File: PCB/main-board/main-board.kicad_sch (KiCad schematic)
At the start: 91 parts, among them J1 AudioJack2_Ground_Switch, J2 AudioJack2_Ground_Switch, J3 AudioJack2_Ground_Switch, J4 AudioJack2_Ground_Switch, J5 AudioJack2_Ground_Switch, J6 Conn_01x14, J7 Conn_01x03, Q1 Si1308EDL, Q10 Si1308EDL, Q11 DMG2305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

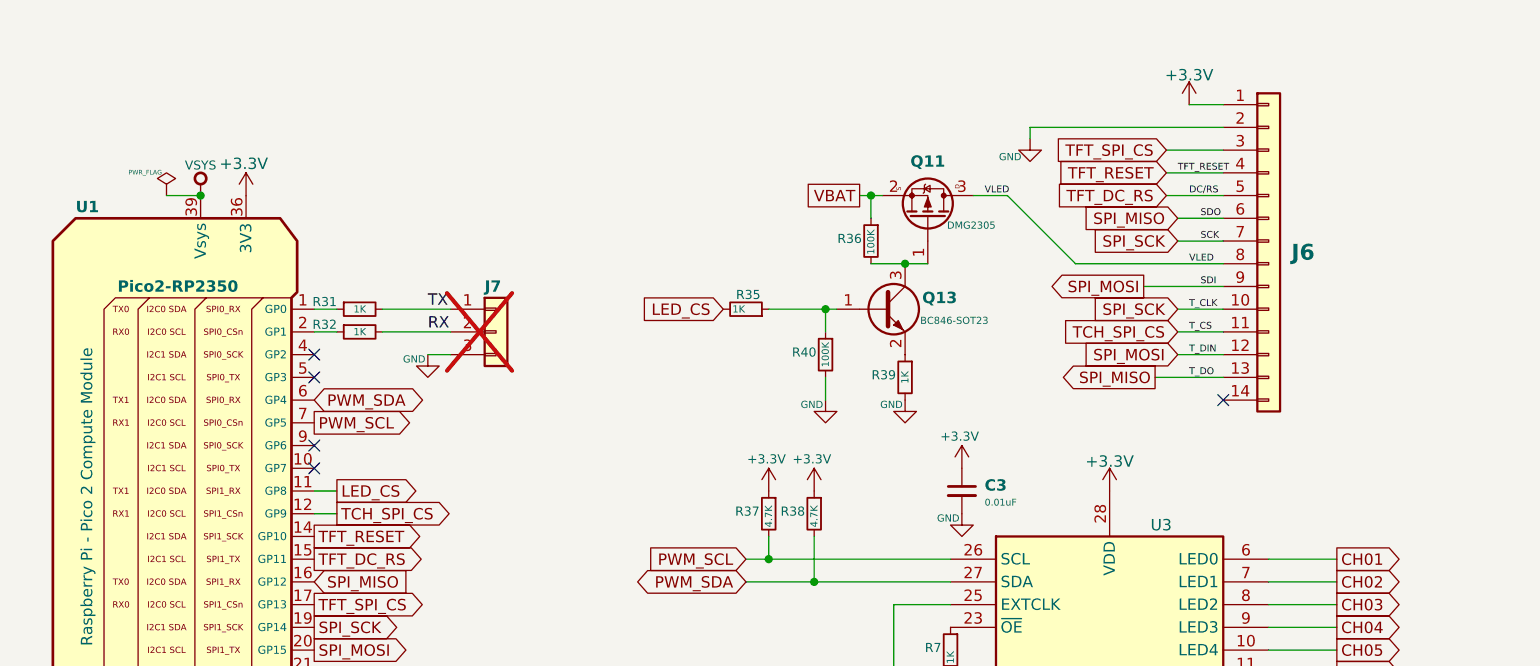
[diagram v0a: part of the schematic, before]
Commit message: Add red-line notes.
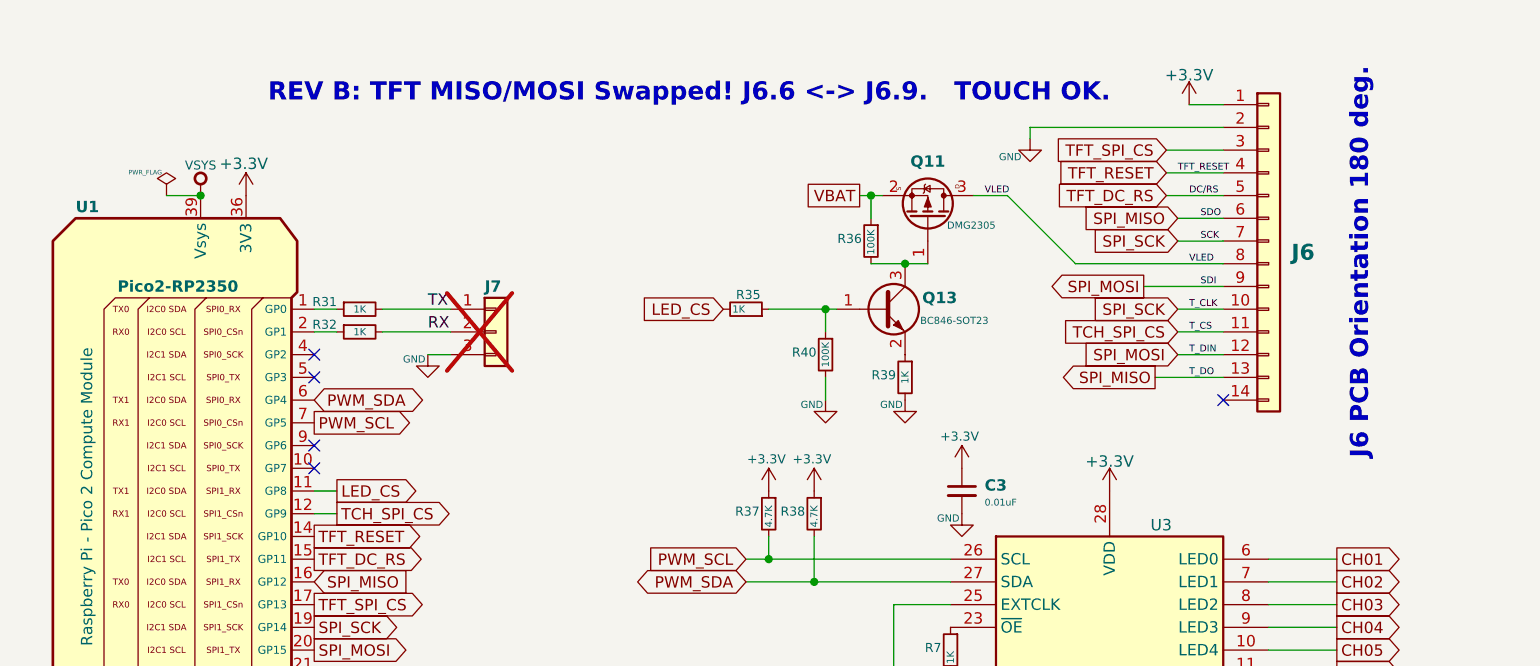
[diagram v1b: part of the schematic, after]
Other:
- note added: "J6 PCB Orientation 180 deg."
- note added: "REV B: TFT MISO/MOSI Swapped! J6.6 <-> J6.9. TOUCH OK."
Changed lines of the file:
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@@
+		)
+	)
+	(text "REV B: TFT MISO/MOSI Swapped! J6.6 <-> J6.9.   TOUCH OK. "
+		(exclude_from_sim no)
+		(at 106.68 17.78 0)
+		(effects
+			(font
+				(size 2.032 2.032)
+				(thickness 0.4064)
+				(bold yes)
+				(color 255 0 0 1)
+			)
 		)
 	)
@@
 			)
 		)
+	)
+	(text "J6 PCB Orientation 180 deg."
+		(exclude_from_sim no)
+		(at 181.61 36.83 90)
+		(effects
+			(font
+				(size 2.032 2.032)
+				(thickness 0.4064)
+				(bold yes)
+				(color 255 0 0 1)
+			)
+		)
